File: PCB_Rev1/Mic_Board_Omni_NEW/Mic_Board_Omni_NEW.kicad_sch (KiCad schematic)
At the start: 31 parts, among them J2 532610771, J3 S2B-ZR-SM4A-TF_LF__SN_, U1 OPA1671IDBVR

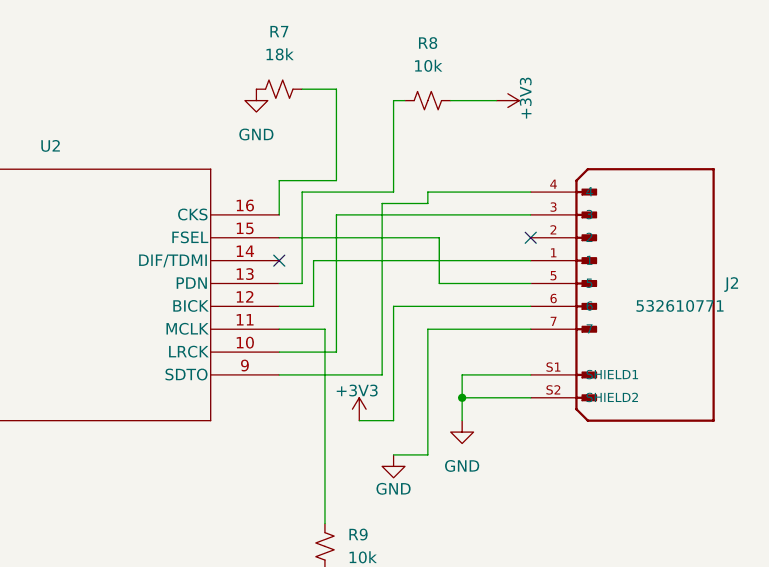
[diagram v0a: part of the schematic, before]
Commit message: new mic boards added
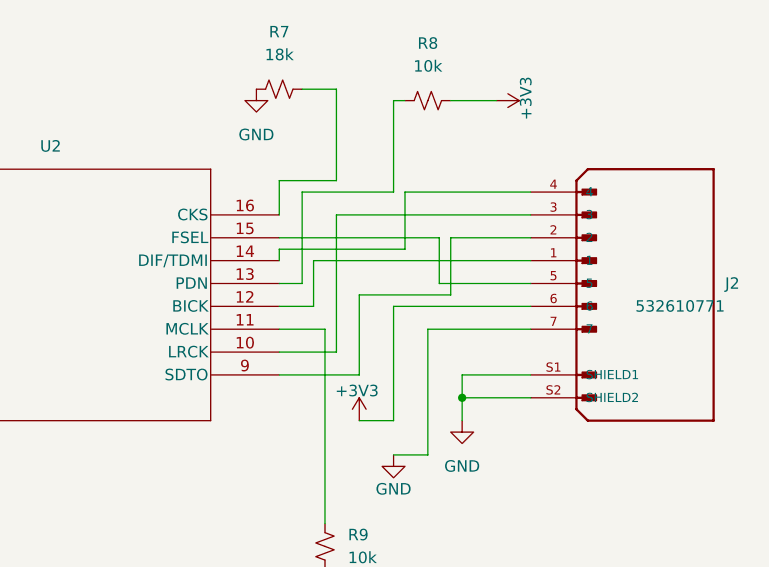
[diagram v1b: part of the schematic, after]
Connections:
- net at J2.2: now also U2.9 (SDTO)
- net at J2.4: now also U2.14 (DIF/TDMI); no longer U2.9 (SDTO)
- no-connect marks 2 -> 0
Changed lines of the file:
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@@
 		(color 0 0 0 0)
 	)
-	(no_connect
-		(at 262.89 86.36)
-	)
-	(no_connect
-		(at 234.95 88.9)
-	)
 	(wire
 		(pts
@@
 	(wire
 		(pts
-			(xy 234.95 101.6) (xy 246.38 101.6)
-		)
-		(stroke
-			(width 0)
-			(type default)
-		)
-	)
-	(wire
-		(pts
 			(xy 262.89 83.82) (xy 241.3 83.82)
 		)
@@
 	(wire
 		(pts
+			(xy 254 86.36) (xy 262.89 86.36)
+		)
+		(stroke
+			(width 0)
+			(type default)
+		)
+	)
+	(wire
+		(pts
 			(xy 247.65 93.98) (xy 262.89 93.98)
 		)
@@
 	(wire
 		(pts
+			(xy 262.89 81.28) (xy 248.92 81.28)
+		)
+		(stroke
+			(width 0)
+			(type default)
+		)
+	)
+	(wire
+		(pts
 			(xy 144.78 109.22) (xy 144.78 88.9)
 		)
@@
 	(wire
 		(pts
+			(xy 248.92 81.28) (xy 248.92 87.63)
+		)
+		(stroke
+			(width 0)
+			(type default)
+		)
+	)
+	(wire
+		(pts
 			(xy 81.28 83.82) (xy 81.28 87.63)
 		)
@@
 	(wire
 		(pts
+			(xy 243.84 101.6) (xy 234.95 101.6)
+		)
+		(stroke
+			(width 0)
+			(type default)
+		)
+	)
+	(wire
+		(pts
 			(xy 81.28 92.71) (xy 81.28 95.25)
 		)
@@
 	(wire
 		(pts
-			(xy 246.38 101.6) (xy 246.38 82.55)
-		)
-		(stroke
-			(width 0)
-			(type default)
-		)
-	)
-	(wire
-		(pts
 			(xy 67.31 83.82) (xy 69.85 83.82)
 		)
@@
 	(wire
 		(pts
+			(xy 248.92 87.63) (xy 234.95 87.63)
+		)
+		(stroke
+			(width 0)
+			(type default)
+		)
+	)
+	(wire
+		(pts
 			(xy 40.64 86.36) (xy 44.45 86.36)
 		)
@@
 	(wire
 		(pts
+			(xy 254 86.36) (xy 254 92.71)
+		)
+		(stroke
+			(width 0)
+			(type default)
+		)
+	)
+	(wire
+		(pts
 			(xy 184.15 101.6) (xy 184.15 106.68)
 		)
@@
 	(wire
 		(pts
+			(xy 243.84 92.71) (xy 243.84 101.6)
+		)
+		(stroke
+			(width 0)
+			(type default)
+		)
+	)
+	(wire
+		(pts
 			(xy 180.34 88.9) (xy 180.34 86.36)
 		)
@@
 	(wire
 		(pts
+			(xy 254 92.71) (xy 243.84 92.71)
+		)
+		(stroke
+			(width 0)
+			(type default)
+		)
+	)
+	(wire
+		(pts
 			(xy 238.76 93.98) (xy 234.95 93.98)
 		)
@@
 	(wire
 		(pts
+			(xy 234.95 87.63) (xy 234.95 88.9)
+		)
+		(stroke
+			(width 0)
+			(type default)
+		)
+	)
+	(wire
+		(pts
 			(xy 154.94 99.06) (xy 154.94 116.84)
 		)
@@
 	(wire
 		(pts
-			(xy 246.38 82.55) (xy 251.46 82.55)
-		)
-		(stroke
-			(width 0)
-			(type default)
-		)
-	)
-	(wire
-		(pts
-			(xy 251.46 82.55) (xy 251.46 81.28)
-		)
-		(stroke
-			(width 0)
-			(type default)
-		)
-	)
-	(wire
-		(pts
 			(xy 152.4 91.44) (xy 160.02 91.44)
 		)
@@
 		)
 		(stroke
-			(width 0)
-			(type default)
-		)
-	)
-	(wire
-		(pts
-			(xy 251.46 81.28) (xy 262.89 81.28)
-		)
-		(stroke

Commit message: MICBOARD OMNI CSV DONE
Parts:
- removed J3: S2B-ZR-SM4A-TF_LF__SN_, Footprints:Mic_Conn, symbol Mic Connectors:S2B-ZR-SM4A-TF_LF__SN_
- added MK1: Microphone, Footprints:Omnidirectional, symbol Device:Microphone
- C1, C10, C8, C9: LCSC (none) -> C519973
- C11: LCSC (none) -> C519977
- C2, C5, C6, C7: LCSC (none) -> C88484
- C3: LCSC (none) -> C576434
- C4: LCSC (none) -> C3857194
- J2: LCSC (none) -> C505276
- R1: LCSC (none) -> C865529
- R2, R8, R9: LCSC (none) -> C110775
- R3, R4: LCSC (none) -> C96346
- R5: LCSC (none) -> C95781
- R6: LCSC (none) -> C868262
- R7: LCSC (none) -> C137468
- U1: LCSC (none) -> C1849409
- U2: LCSC (none) -> C1519002
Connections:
- net GND: now also MK1.1 (-)
- net at C2.1, R2.2: now also MK1.2 (+)
